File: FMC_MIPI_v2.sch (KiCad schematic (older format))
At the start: 0 parts

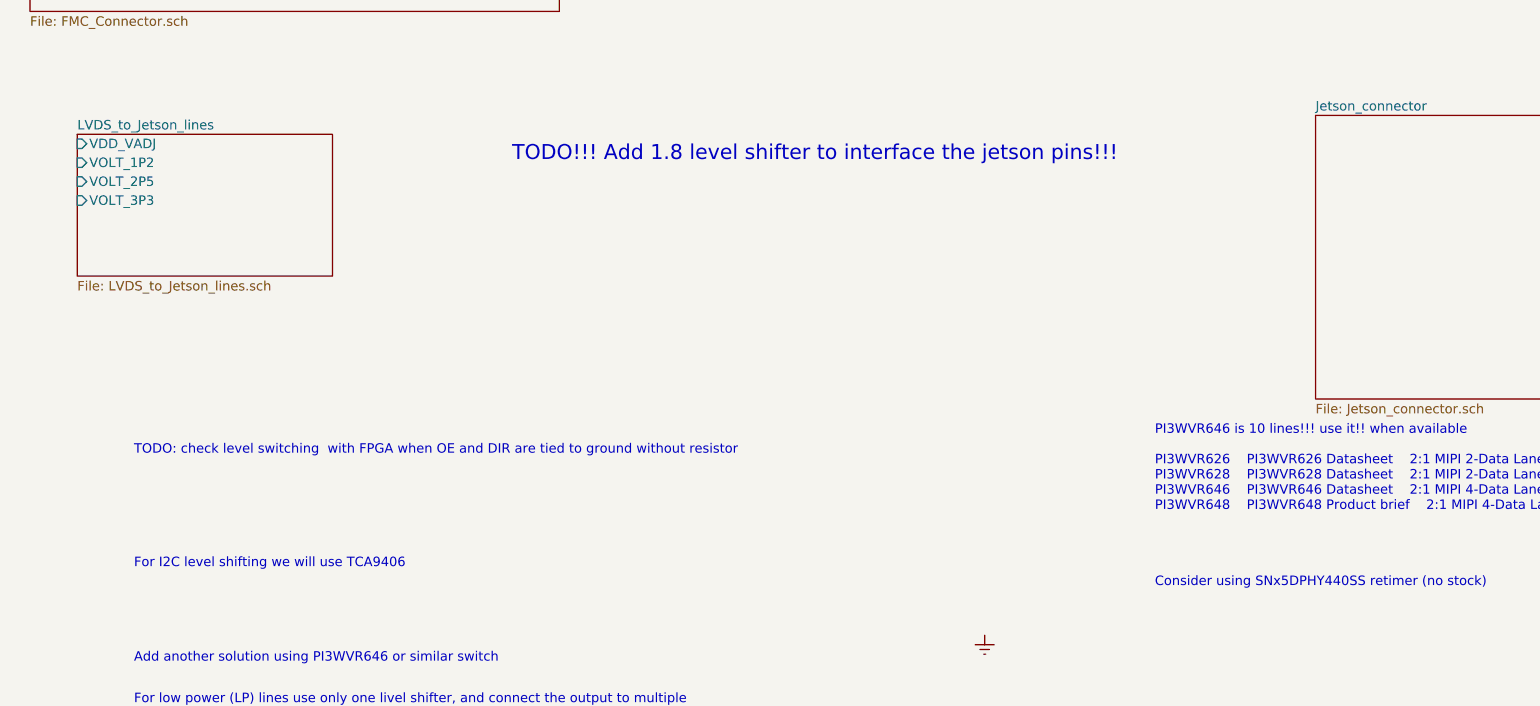
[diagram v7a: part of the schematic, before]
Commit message: added more level shifters and power 1.8 Volt
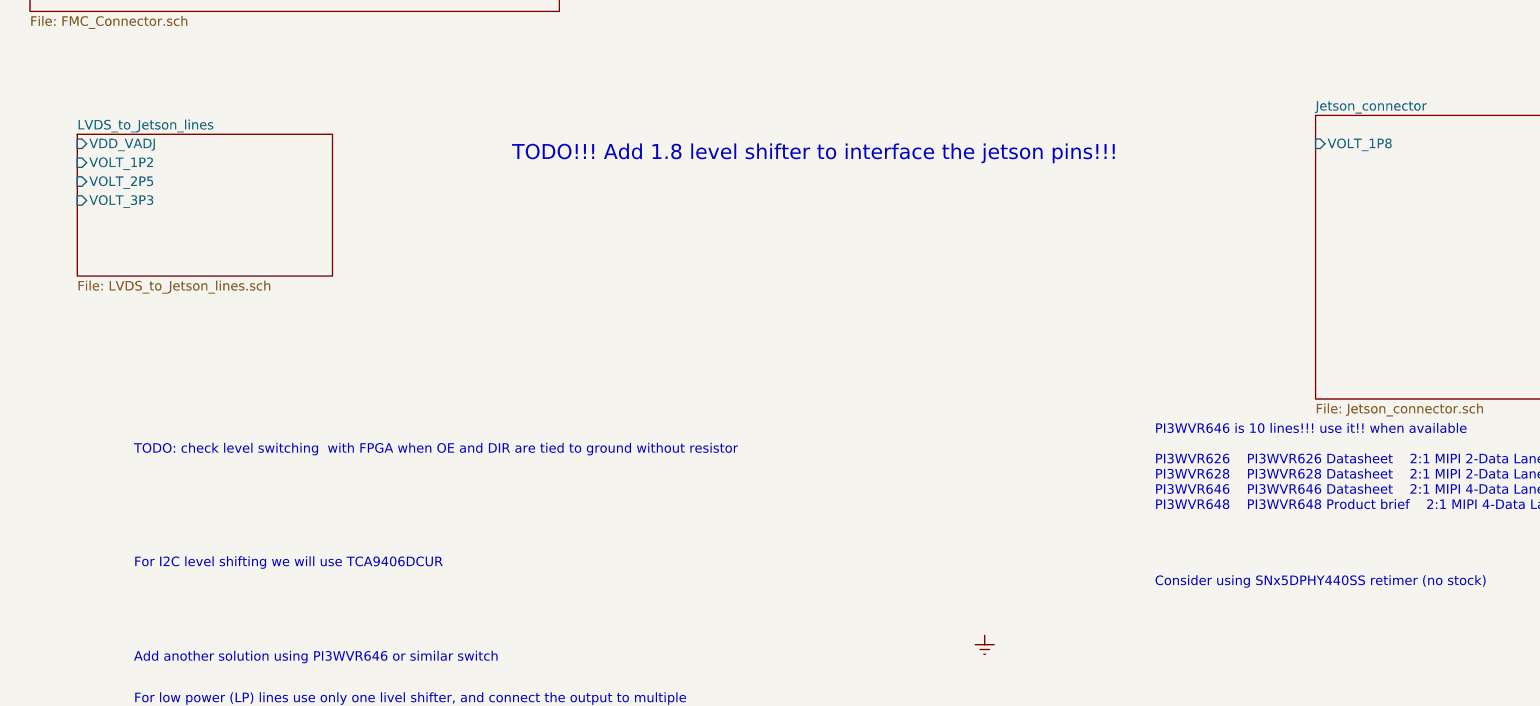
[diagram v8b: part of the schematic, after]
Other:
- note added: "For I2C level shifting we will use TCA9406DCUR"
- note removed: "For I2C level shifting we will use TCA9406"
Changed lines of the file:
@@
 F0 "Jetson_connector" 50
 F1 "Jetson_connector.sch" 50
+F2 "VOLT_1P8" I L 7700 3000 50
 $EndSheet
 $Comp
@@
 TODO: check level switching  with FPGA when OE and DIR are tied to ground without resistor
 Text Notes 1450 5250 0    50   ~ 0
-For I2C level shifting we will use TCA9406
+For I2C level shifting we will use TCA9406DCUR
 Text Notes -100 -400 0    118  ~ 0
 To switch cameras simply use: TS5MP645\n\nhttps://www.ti.com/lit/ds/symlink/ts5mp645.pdf?ts=1639239156409&ref_url=https%253A%252F%252Fwww.ti.com%252Fproduct%252FTS5MP645
